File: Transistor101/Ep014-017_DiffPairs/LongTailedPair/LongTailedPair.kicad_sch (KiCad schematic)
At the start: 14 parts, among them J1 AWG channel 1, J2 AWG channel 2, J3 Output to oscilloscope, Q1 DMMT5551, T1 SEE NOTES

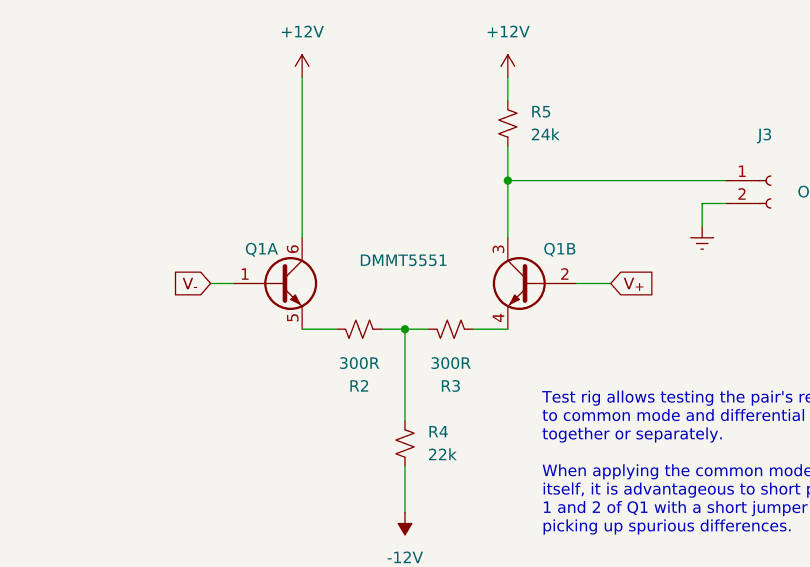
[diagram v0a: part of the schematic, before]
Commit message: Correct pinout of DMMT5401
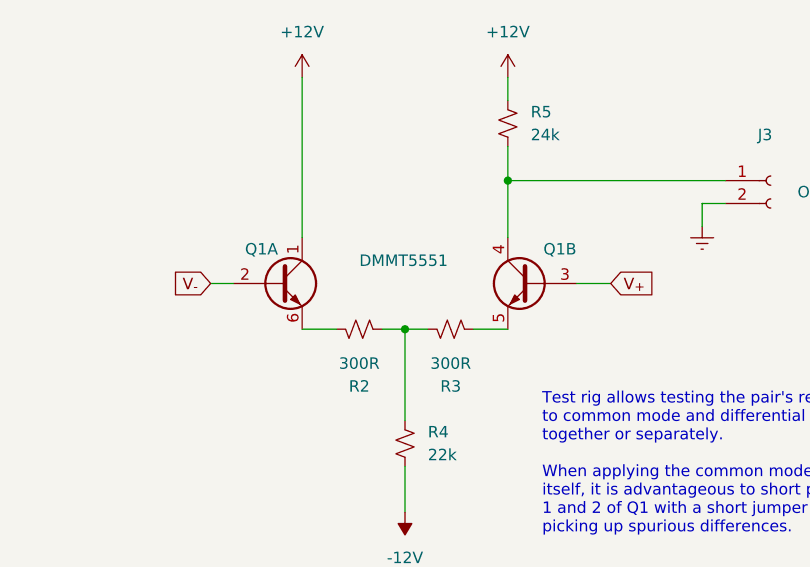
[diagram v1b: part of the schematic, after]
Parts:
- Q1: footprint (none) -> Package_TO_SOT_SMD:SOT-363_SC-70-6; symbol Kevin-Transistors:Q_Dual_NPN_NPN_B1B2C2E2E1C1 -> Kevin-Transistors:DMMT5551
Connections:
- net +12V: now also Q1.1 (C1); no longer Q1.6 (C1)
- net V_{+}: now also Q1.3 (B2); no longer Q1.2 (B2)
- net V_{-}: now also Q1.2 (B1); no longer Q1.1 (B1)
- net at R2.1: now also Q1.6 (E1); no longer Q1.5 (E1)
- net at J3.1 (Pin_1), R5.2: now also Q1.4 (C2); no longer Q1.3 (C2)
- net at R3.2: now also Q1.5 (E2); no longer Q1.4 (E2)
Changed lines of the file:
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@@
   (title_block
     (title "Long-tailed pair: the basic circuit")
-    (date "2025-01-27")
-    (rev "A")
+    (date "2026-05-13")
+    (rev "B")
     (company "Kludges from Kevin's Cave")
     (comment 1 "The differential pair: the heart of analog circuits")
@@
     )
   )
-  (symbol (lib_id "Kevin-Transistors:Q_Dual_NPN_NPN_B1B2C2E2E1C1") (at 176.53 72.39 0) (mirror y) (unit 2)
+  (symbol (lib_id "Kevin-Transistors:DMMT5551") (at 176.53 72.39 0) (mirror y) (unit 2)
     (in_bom yes) (on_board yes) (dnp no)
     (property "Reference" "Q1" (at 181.61 68.58 0)
@@
       (effects (font (size 1.27 1.27)) (justify left) hide)
     )
-    (property "Footprint" "" (at 171.45 69.85 0)
-      (effects (font (size 1.27 1.27)) hide)
-    )
-    (property "Datasheet" "~" (at 176.53 72.39 0)
+    (property "Footprint" "Package_TO_SOT_SMD:SOT-363_SC-70-6" (at 171.45 69.85 0)
+      (effects (font (size 1.27 1.27)) hide)
+    )
+    (property "Datasheet" "https://www.diodes.com/assets/Datasheets/ds30436.pdf" (at 176.53 72.39 0)
       (effects (font (size 1.27 1.27)) hide)
     )
@@
     )
   )
-  (symbol (lib_id "Kevin-Transistors:Q_Dual_NPN_NPN_B1B2C2E2E1C1") (at 148.59 72.39 0) (unit 1)
+  (symbol (lib_id "Kevin-Transistors:DMMT5551") (at 148.59 72.39 0) (unit 1)
     (in_bom yes) (on_board yes) (dnp no)
     (property "Reference" "Q1" (at 144.78 68.58 0)
@@
       (effects (font (size 1.27 1.27)) (justify left))
     )
-    (property "Footprint" "" (at 153.67 69.85 0)
-      (effects (font (size 1.27 1.27)) hide)
-    )
-    (property "Datasheet" "~" (at 148.59 72.39 0)
-      (effects (font (size 1.27 1.27)) hide)
-    )
+    (property "Footprint" "Package_TO_SOT_SMD:SOT-363_SC-70-6" (at 153.67 69.85 0)
+      (effects (font (size 1.27 1.27)) hide)
+    )
+    (property "Datasheet" "https://www.diodes.com/assets/Datasheets/ds30436.pdf" (at 148.59 72.39 0)
+      (effects (font (size 1.27 1.27)) hide)
+    )
